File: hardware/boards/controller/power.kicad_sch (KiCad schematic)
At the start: 11 parts, among them J1 01x02, J8 01x03, SW2 Power, U2 AMS1117-5.0, U3 AMS1117-3.3

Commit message: new version for pcb controller
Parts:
- removed SW2: Power, switch:SW_Slide9.1x3.5, symbol common:Switch
- added D4, D5: Diode, common:D_SOD123FL, symbol common:Diode
- added SW5: Power, switch:SW_Slide9.1x3.5, symbol common:SW_Slide
- D2: renamed from D3; footprint common:D_SOD123 -> common:D_SOD123FL; Ext. Price 0.20 -> 0.29; LCSC Part C2892681 -> C18199085; Manufacturer YONGYUTAI -> R+O; Manufacturer Part 1N4007 -> 1N4001W; Unit Price 0.004 -> 0.0057
- J4: renamed from J8; now left out of the parts list
- J5: renamed from J1; now left out of the parts list
- renumbered C5 to C7, C6 to C8, C4 to C9, D1 to D3, R17 to R19, U2 to U3, U3 to U4
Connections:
- net +3.3V: now also D5.1 (K); no longer C8.1, U4.2 (VOUT)
- net +5V: now also D4.1 (K); no longer C7.1, U3.2 (VOUT)
- net GND: now also D3.1 (K), J5.1; no longer J5.2, R19.1
- net at D2.2 (A): now also R19.2, SW5.2; no longer D3.2 (A)
- new net: C7.1, D4.2 (A), U3.2 (VOUT)
- new net: C8.1, D5.2 (A), U4.2 (VOUT)
- new net: J5.2, SW5.3
- new net: D3.2 (A), R19.1
- no-connect marks 0 -> 1
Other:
- moved on the sheet: C7, C8, C9, D2, D3, J4, J5, R19, U3, U4

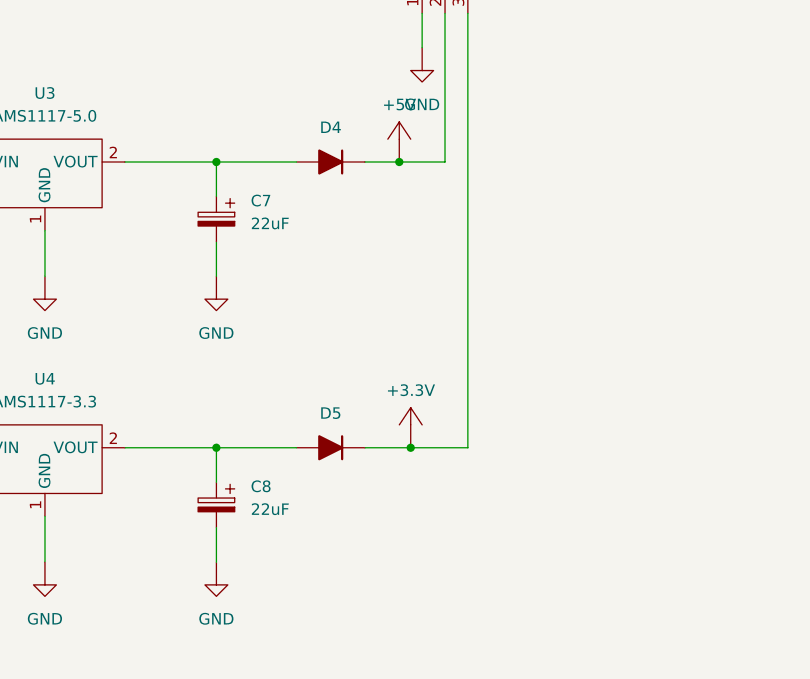
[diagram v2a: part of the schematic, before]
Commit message: change kicad default to custom
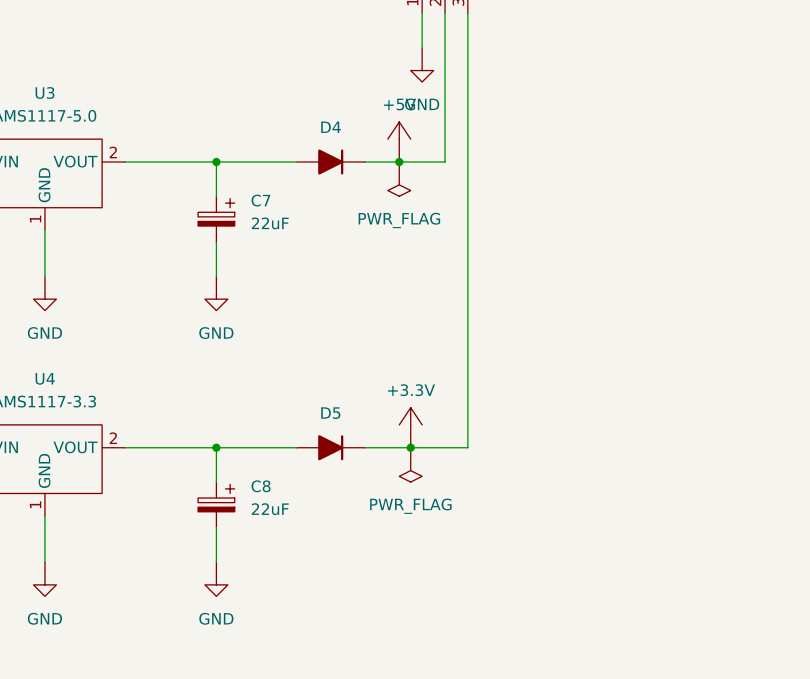
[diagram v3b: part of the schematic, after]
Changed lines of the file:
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@@
+	)
+	(symbol
+		(lib_id "pwr:PWR_FLAG")
+		(at 173.99 97.79 180)
+		(unit 1)
+		(exclude_from_sim no)
+		(in_bom no)
+		(on_board no)
+		(dnp no)
+		(fields_autoplaced yes)
+		(property "Reference" "#FLAG04"
+			(at 173.99 102.29 0)
+			(effects
+				(font
+					(size 1.27 1.27)
+				)
+				(hide yes)
+			)
+		)
+		(property "Value" "PWR_FLAG"
+			(at 173.99 101.6 0)
+			(effects
+				(font
+					(size 1.27 1.27)
+				)
+			)
+		)
+		(property "Footprint" ""
+			(at 173.99 97.79 0)
+			(effects
+				(font
+					(size 1.27 1.27)
+				)
+				(hide yes)
+			)
+		)
+		(property "Datasheet" ""
+			(at 173.99 97.79 0)
+			(effects
+				(font
+					(size 1.27 1.27)
+				)
+				(hide yes)
+			)
+		)
+		(property "Description" "Power Flag"
+			(at 173.99 85.29 0)
+			(effects
+				(font
+					(size 1.27 1.27)
+				)
+				(hide yes)
+			)
+		)
+		(pin "1"
+		)
+		(instances
+			(project ""
+				(path "/beaf00ba-d60c-407c-adfe-9d518bae0b16/c4e35d3f-6040-4882-878d-1a95fa713f03"
+					(reference "#FLAG04")
+					(unit 1)
+				)
+			)
+		)
 	)
 	(symbol
@@
 					(unit 1)
 				)
+			)
+		)
+	)
+	(symbol
+		(lib_id "pwr:PWR_FLAG")
+		(at 172.72 66.04 180)
+		(unit 1)
+		(exclude_from_sim no)
+		(in_bom no)
+		(on_board no)
+		(dnp no)
+		(fields_autoplaced yes)
+		(property "Reference" "#FLAG03"
+			(at 172.72 70.54 0)
+			(effects
+				(font
+					(size 1.27 1.27)
+				)
+				(hide yes)
+			)
+		)
+		(property "Value" "PWR_FLAG"
+			(at 172.72 69.85 0)
+			(effects
+				(font
+					(size 1.27 1.27)
+				)
+			)
+		)
+		(property "Footprint" ""
+			(at 172.72 66.04 0)
+			(effects
+				(font
+					(size 1.27 1.27)
+				)
+				(hide yes)
+			)
+		)
+		(property "Datasheet" ""
+			(at 172.72 66.04 0)
+			(effects
+				(font
+					(size 1.27 1.27)
+				)
+				(hide yes)
+			)
+		)
+		(property "Description" "Power Flag"
+			(at 172.72 53.54 0)
+			(effects
+				(font
+					(size 1.27 1.27)
+				)
+				(hide yes)
+			)
+		)
+		(pin "1"
+		)
+		(instances
+			(project ""
+				(path "/beaf00ba-d60c-407c-adfe-9d518bae0b16/c4e35d3f-6040-4882-878d-1a95fa713f03"
+					(reference "#FLAG03")
+					(unit 1)
+				)
